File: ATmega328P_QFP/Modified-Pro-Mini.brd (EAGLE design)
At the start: 17.8 x 33 mm, 25 parts, among them Q1 8/16/20MHz, U1 ATMEGA328, U2 MIC5205

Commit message: updated silk
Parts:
- removed U$1: LOGO-SFESK, SparkFun:SFE-LOGO-FLAME
- removed U$11: LOGO-SFENEW, SparkFun:SFE-NEW-WEBLOGO
- removed U$3: OSHW-LOGOS, SparkFun:OSHW-LOGO-S
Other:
- board text removed: "Arduino Pro"
- board text removed: "Mini"
- board text removed: "www.arduino.cc"
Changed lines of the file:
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@@
 <grid distance="0.05" unitdist="inch" unit="inch" style="lines" multiple="1" display="yes" altdistance="0.005" altunitdist="inch" altunit="inch"/>
 <layers>
-<layer number="1" name="Top" color="4" fill="1" visible="yes" active="yes"/>
+<layer number="1" name="Top" color="4" fill="1" visible="no" active="yes"/>
 <layer number="2" name="Route2" color="1" fill="3" visible="no" active="no"/>
 <layer number="3" name="Route3" color="4" fill="3" visible="no" active="no"/>
@@
 <text x="1.27" y="30.734" size="0.8128" layer="21" ratio="15" rot="R90">BLK</text>
 <text x="17.272" y="30.734" size="0.8128" layer="21" ratio="15" rot="R90">GRN</text>
-<text x="6.5532" y="27.4574" size="0.8128" layer="21" ratio="15">Arduino Pro</text>
-<text x="8.636" y="28.575" size="0.8128" layer="21" ratio="15">Mini</text>
-<text x="4.191" y="6.858" size="1.778" layer="22" ratio="15" rot="MR90">www.arduino.cc</text>
 <text x="19.812" y="26.162" size="1.27" layer="27">Valid combinations:</text>
 <text x="19.812" y="23.622" size="1.27" layer="27">168V / 3.3V Reg / 8MHz</text>
@@
 <attribute name="VALUE" x="13.0556" y="0.9784" size="0.4064" layer="27" rot="R90"/>
 </element>
-<element name="U$11" library="SparkFun" package="SFE-NEW-WEBLOGO" value="LOGO-SFENEW" x="7.112" y="7.239" rot="MR90"/>
 <element name="U2" library="SparkFun" package="SOT23-5" value="MIC5205" x="8.89" y="24.1808" smashed="yes" rot="R90">
 <attribute name="NAME" x="6.731" y="23.2918" size="0.4064" layer="25" rot="R90"/>
@@
 <element name="JP6" library="SparkFun" package="1X12" value="" x="16.51" y="29.21" rot="MR270"/>
 <element name="JP7" library="SparkFun" package="1X12" value="" x="1.27" y="1.27" rot="MR90"/>
-<element name="U$1" library="SparkFun" package="SFE-LOGO-FLAME" value="LOGO-SFESK" x="4.064" y="6.985"/>
 <element name="JP2" library="SparkFun" package="1X02" value="" x="13.589" y="17.907" rot="MR90"/>
 <element name="U1" library="SparkFun" package="TQFP32-08" value="ATMEGA328" x="8.89" y="13.97" smashed="yes" rot="R315">
@@
 </element>
 <element name="JP1" library="SparkFun" package="1X06" value="FTDI Basic" x="15.24" y="31.75" rot="MR0"/>
-<element name="U$3" library="SparkFun" package="OSHW-LOGO-S" value="OSHW-LOGOS" x="12.5984" y="26.3906" rot="MR90"/>
 <element name="R1" library="SparkFun" package="0603-RES" value="" x="12.9794" y="23.1648" rot="MR90"/>
 <element name="R3" library="SparkFun" package="0603-RES" value="" x="14.2494" y="23.1648" rot="MR90"/>

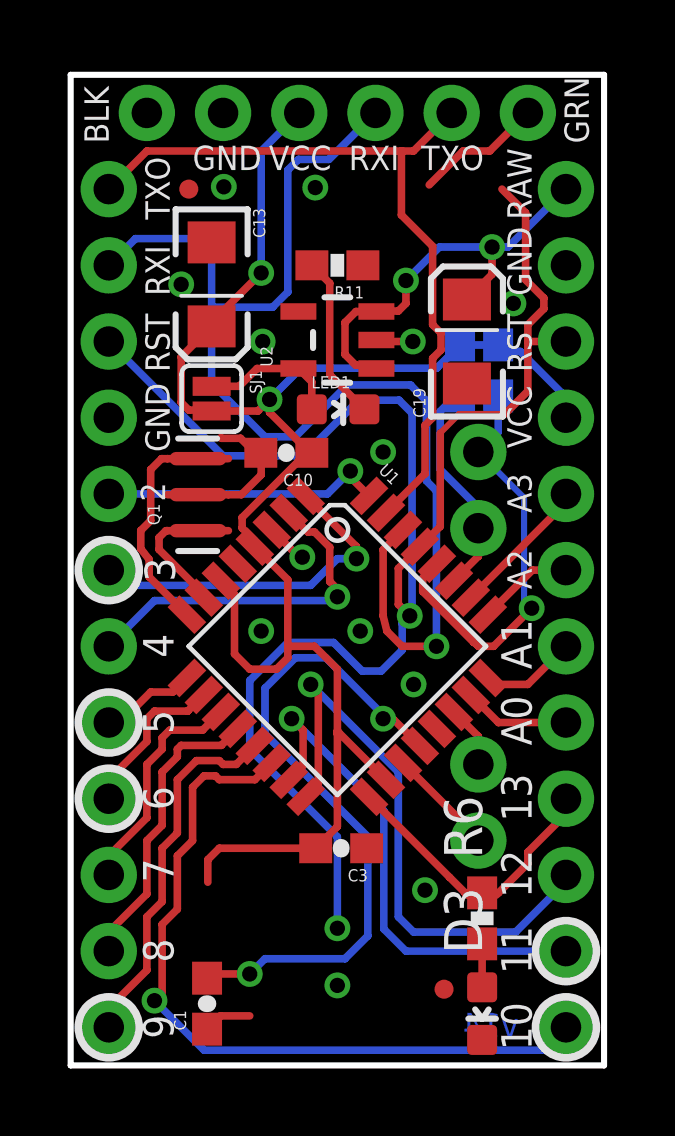
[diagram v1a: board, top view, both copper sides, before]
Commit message: removed power regulator
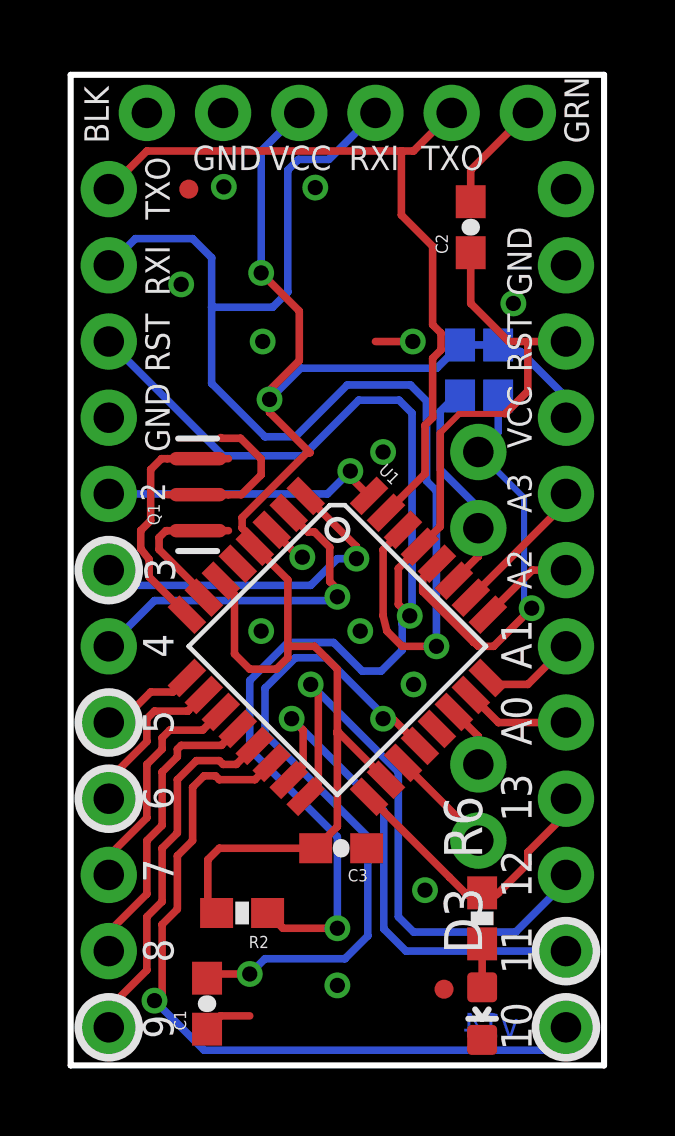
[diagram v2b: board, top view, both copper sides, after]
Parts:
- removed C10: 0.1uF, SparkFun:0603-CAP
- removed C13, C19: 10uF, SparkFun:EIA3216
- removed LED1: Red, Testing:0603-LED-ALT1
- removed R11: 10K, SparkFun:0603-RES
- removed SJ1: (no value), SparkFun-Passives:SJ_2S
- removed U2: MIC5205, SparkFun:SOT23-5
- added C2: 0.1uF, SparkFun:0603-CAP
- added R2: 10K, SparkFun:0603-RES
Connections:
- removed net N$3: LED1.A, SJ1.1, U2.5
- removed net N$4: LED1.C, R11.2
- removed net RAW: C19.A, JP6.1, U2.1, U2.3
- net DTR: now also C2.2
- net GND: no longer C10.2, C13.C, C19.C, R11.1, U2.2
- net RESET: now also C2.1, R2.1
- net VCC: now also R2.2; no longer C10.1, C13.A, SJ1.2
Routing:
- net RAW: track 14.1 -> 0.00 mm, vias 2 -> 0
- net N$4: track 5.53 -> 0.00 mm
- net N$3: track 4.68 -> 0.00 mm
- net VCC: track 57.4 -> 55.0 mm
- net RESET: track 55.6 -> 56.3 mm
- net DTR: track 4.28 -> 3.75 mm
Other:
- board text removed: "RAW"

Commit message: rerouted wires left by removed compoents
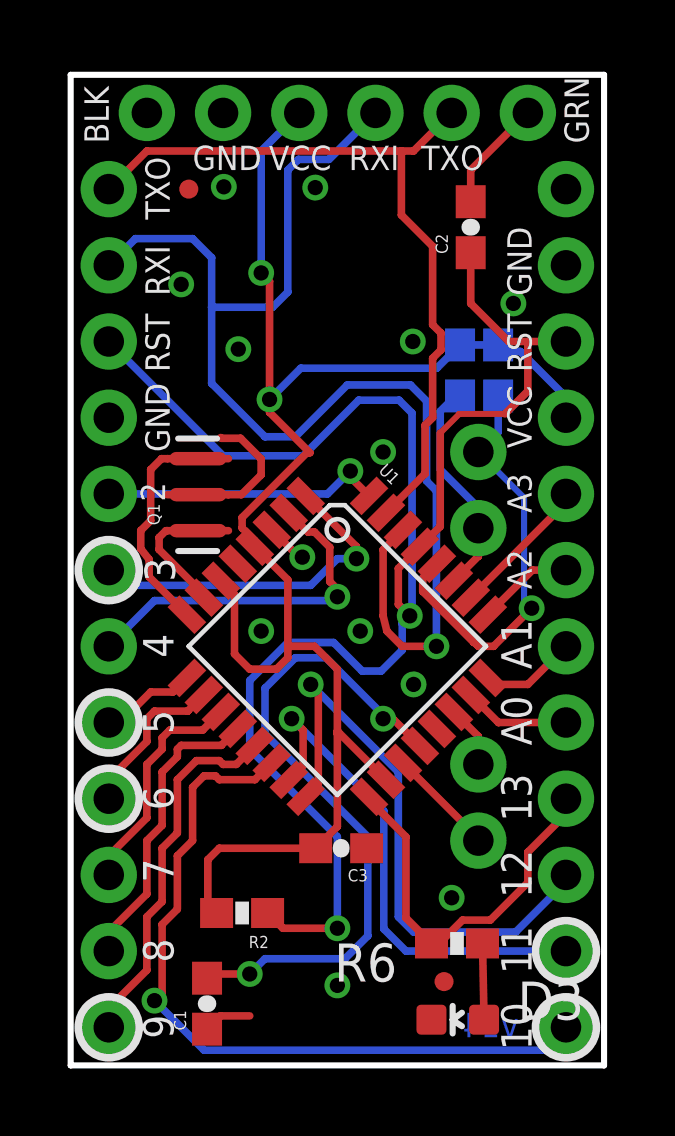
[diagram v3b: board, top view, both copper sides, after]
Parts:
- moved R6 1.19 mm to (12.9, 4.06), turned to 0 degrees
- moved D3 0.84 mm to (12.9, 1.52), turned to 90 degrees
- moved JP8 0.25 mm to (12.4, 2.79)
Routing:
- net SCK: track 9.93 -> 13.5 mm
- net GND: track 7.83 -> 6.59 mm
- net N$7: track 1.45 -> 2.54 mm
- net VCC: track 55.0 -> 54.4 mm
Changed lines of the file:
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@@
 <setting verticaltext="up"/>
 </settings>
-<grid distance="0.02" unitdist="inch" unit="inch" style="lines" multiple="1" display="yes" altdistance="0.005" altunitdist="inch" altunit="inch"/>
+<grid distance="0.01" unitdist="inch" unit="inch" style="lines" multiple="1" display="yes" altdistance="0.005" altunitdist="inch" altunit="inch"/>
 <layers>
 <layer number="1" name="Top" color="4" fill="1" visible="yes" active="yes"/>
@@
 <layer number="19" name="Unrouted" color="6" fill="1" visible="yes" active="yes"/>
 <layer number="20" name="Dimension" color="6" fill="1" visible="yes" active="yes"/>
-<layer number="21" name="tPlace" color="16" fill="1" visible="no" active="yes"/>
-<layer number="22" name="bPlace" color="14" fill="1" visible="no" active="yes"/>
+<layer number="21" name="tPlace" color="16" fill="1" visible="yes" active="yes"/>
+<layer number="22" name="bPlace" color="14" fill="1" visible="yes" active="yes"/>
 <layer number="23" name="tOrigins" color="15" fill="1" visible="yes" active="yes"/>
 <layer number="24" name="bOrigins" color="15" fill="1" visible="yes" active="yes"/>
@@
 <attribute name="VALUE" x="5.5372" y="1.2827" size="0.4064" layer="27" rot="R90"/>
 </element>
-<element name="R6" library="SparkFun" package="0603-RES" value="330" x="13.716" y="4.9022" smashed="yes" rot="R270">
-<attribute name="NAME" x="13.716" y="6.9022" size="1.27" layer="25" rot="R90"/>
-<attribute name="VALUE" x="13.081" y="4.5598" size="0.4064" layer="27" rot="R90"/>
+<element name="R6" library="SparkFun" package="0603-RES" value="330" x="12.8778" y="4.064" smashed="yes">
+<attribute name="NAME" x="10.8778" y="4.064" size="1.27" layer="25" rot="R180"/>
+<attribute name="VALUE" x="13.2202" y="3.429" size="0.4064" layer="27" rot="R180"/>
 </element>
-<element name="D3" library="Testing" package="0603-LED-ALT1" value="Green" x="13.716" y="1.7272" smashed="yes" rot="R180">
-<attribute name="NAME" x="13.716" y="3.7272" size="1.27" layer="25" rot="R90"/>
-<attribute name="VALUE" x="13.0556" y="0.9784" size="0.4064" layer="27" rot="R90"/>
+<element name="D3" library="Testing" package="0603-LED-ALT1" value="Green" x="12.9032" y="1.524" smashed="yes" rot="R90">
+<attribute name="NAME" x="14.9032" y="1.524" size="1.27" layer="25"/>
+<attribute name="VALUE" x="12.1544" y="2.1844" size="0.4064" layer="27"/>
 </element>
 <element name="JP6" library="SparkFun" package="1X12" value="" x="16.51" y="29.21" rot="MR270"/>
@@
 <element name="R3" library="SparkFun" package="0603-RES" value="" x="14.2494" y="23.1648" rot="MR90"/>
 <element name="JP5" library="SparkFun" package="MICRO-FIDUCIAL" value="FIDUCIALUFIDUCIAL" x="3.937" y="29.21"/>
-<element name="JP8" library="SparkFun" package="MICRO-FIDUCIAL" value="FIDUCIALUFIDUCIAL" x="12.446" y="2.54"/>
+<element name="JP8" library="SparkFun" package="MICRO-FIDUCIAL" value="FIDUCIALUFIDUCIAL" x="12.446" y="2.794"/>
 <element name="JP3" library="SparkFun" package="1X02" value="" x="13.589" y="7.493" rot="MR90"/>
 <element name="Q1" library="Testing" package="RESONATOR-SMD-1:1" value="8/16/20MHz" x="4.2418" y="19.0246" rot="R90"/>
@@
 <contactref element="JP1" pad="5"/>
 <contactref element="JP1" pad="6"/>
-<wire x1="11.4046" y1="24.13" x2="10.16" y2="24.13" width="0.254" layer="1"/>
 <via x="11.43" y="12.7" extent="1-16" drill="0.508"/>
 <via x="9.652" y="14.478" extent="1-16" drill="0.508"/>
@@
 <via x="3.683" y="26.035" extent="1-16" drill="0.508"/>
 <via x="11.4046" y="24.13" extent="1-16" drill="0.508"/>
-<via x="6.4008" y="24.13" extent="1-16" drill="0.508"/>
 <polygon width="0.254" layer="1" isolate="0.3048">
 <vertex x="0" y="33.02"/>
@@
 <wire x1="7.666053125" y1="16.891" x2="7.747" y2="16.891" width="0.254" layer="1"/>
 <via x="8.1534" y="29.2608" extent="1-16" drill="0.508"/>
-<via x="11.811" y="5.842" extent="1-16" drill="0.508"/>
 <contactref element="Q1" pad="2"/>
 <wire x1="5.2578" y1="19.0246" x2="5.6896" y2="19.0246" width="0.254" layer="1"/>
@@
 <wire x1="5.6642" y1="20.9042" x2="5.0292" y2="20.9042" width="0.254" layer="1"/>
 <wire x1="5.0292" y1="20.9042" x2="5.0038" y2="20.9296" width="0.254" layer="1"/>
+<via x="5.588" y="23.876" extent="1-16" drill="0.508"/>
+<via x="12.7" y="5.588" extent="1-16" drill="0.508"/>
 </signal>
 <signal name="AREF">
@@
 <wire x1="16.51" y1="8.382" x2="16.51" y2="8.89" width="0.254" layer="1"/>
 <wire x1="15.24" y1="7.112" x2="16.51" y2="8.382" width="0.254" layer="1"/>
-<wire x1="15.24" y1="6.731" x2="15.24" y2="7.112" width="0.254" layer="1"/>
-<wire x1="14.185" y1="5.676" x2="14.2612" y2="5.7522" width="0.254" layer="1"/>
-<wire x1="9.945425" y1="8.954771875" x2="12.6251" y2="6.275096875" width="0.254" layer="1"/>
-<wire x1="13.147996875" y1="5.7522" x2="13.224196875" y2="5.676" width="0.254" layer="1"/>
-<wire x1="13.716" y1="5.7522" x2="14.2612" y2="5.7522" width="0.254" layer="1"/>
-<wire x1="14.2612" y1="5.7522" x2="15.24" y2="6.731" width="0.254" layer="1"/>
-<wire x1="13.716" y1="5.7522" x2="13.147996875" y2="5.7522" width="0.254" layer="1"/>
-<wire x1="13.147996875" y1="5.7522" x2="12.6251" y2="6.275096875" width="0.254" layer="1"/>
+<wire x1="11.938" y1="4.1538" x2="12.0278" y2="4.064" width="0.254" layer="1"/>
+<wire x1="12.0278" y1="4.064" x2="12.28266875" y2="4.064" width="0.254" layer="1"/>
+<wire x1="9.945425" y1="8.954771875" x2="9.945425" y2="8.850575" width="0.254" layer="1"/>
+<wire x1="9.945425" y1="8.850575" x2="11.176" y2="7.62" width="0.254" layer="1"/>
+<wire x1="11.176" y1="7.62" x2="11.176" y2="4.9158" width="0.254" layer="1"/>
+<wire x1="11.176" y1="4.9158" x2="12.0278" y2="4.064" width="0.254" layer="1"/>
+<wire x1="13.06206875" y1="4.8434" x2="13.9874" y2="4.8434" width="0.254" layer="1"/>
+<wire x1="13.9874" y1="4.8434" x2="15.24" y2="6.096" width="0.254" layer="1"/>
+<wire x1="12.0278" y1="4.064" x2="12.28266875" y2="4.064" width="0.254" layer="1"/>
+<wire x1="12.28266875" y1="4.064" x2="13.06206875" y2="4.8434" width="0.254" layer="1"/>
+<wire x1="15.24" y1="6.096" x2="15.24" y2="7.112" width="0.254" layer="1"/>
 </signal>
 <signal name="MISO">
@@
 <contactref element="R6" pad="2"/>
 <contactref element="D3" pad="A"/>
-<wire x1="13.716" y1="2.6042" x2="13.716" y2="4.0522" width="0.254" layer="1"/>
+<wire x1="13.7802" y1="1.524" x2="13.7278" y2="4.064" width="0.254" layer="1"/>
 </signal>
 <signal name="TXO">
@@
 <wire x1="6.6294" y1="21.7678" x2="6.6294" y2="22.1996" width="0.254" layer="1"/>
 <wire x1="6.6294" y1="22.1996" x2="6.6294" y2="22.5044" width="0.254" layer="1"/>
-<wire x1="6.6294" y1="22.5044" x2="7.62" y2="23.495" width="0.254" layer="1"/>
-<wire x1="7.62" y1="23.495" x2="7.62" y2="25.146" width="0.254" layer="1"/>
-<wire x1="7.62" y1="25.146" x2="6.35" y2="26.416" width="0.254" layer="1"/>
 <contactref element="R2" pad="2"/>
 <wire x1="4.572" y1="6.858" x2="4.572" y2="5.373" width="0.254" layer="1"/>
 <wire x1="4.572" y1="5.373" x2="4.865" y2="5.08" width="0.254" layer="1"/>
 <wire x1="7.874" y1="20.4216" x2="7.9756" y2="20.4216" width="0.254" layer="1"/>
+<wire x1="6.6294" y1="22.1996" x2="6.6294" y2="26.1366" width="0.254" layer="1"/>
+<wire x1="6.6294" y1="26.1366" x2="6.35" y2="26.416" width="0.254" layer="1"/>
 </signal>
 <signal name="D9">

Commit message: changed raw pin to gnd
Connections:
- net GND: now also JP6.1
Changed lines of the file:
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@@
 <via x="5.588" y="23.876" extent="1-16" drill="0.508"/>
 <via x="12.7" y="5.588" extent="1-16" drill="0.508"/>
+<contactref element="JP6" pad="1"/>
 </signal>
 <signal name="AREF">

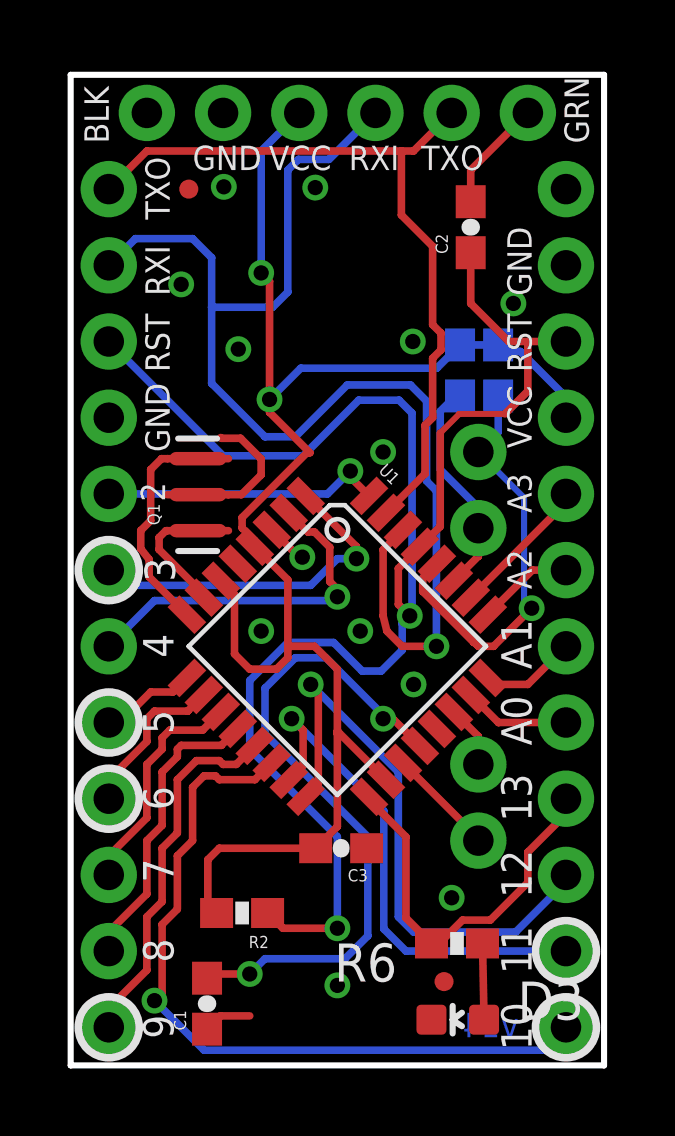
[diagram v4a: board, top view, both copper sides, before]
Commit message: bumbed out all sides by 0.01in
got board to pass OSH park DRC
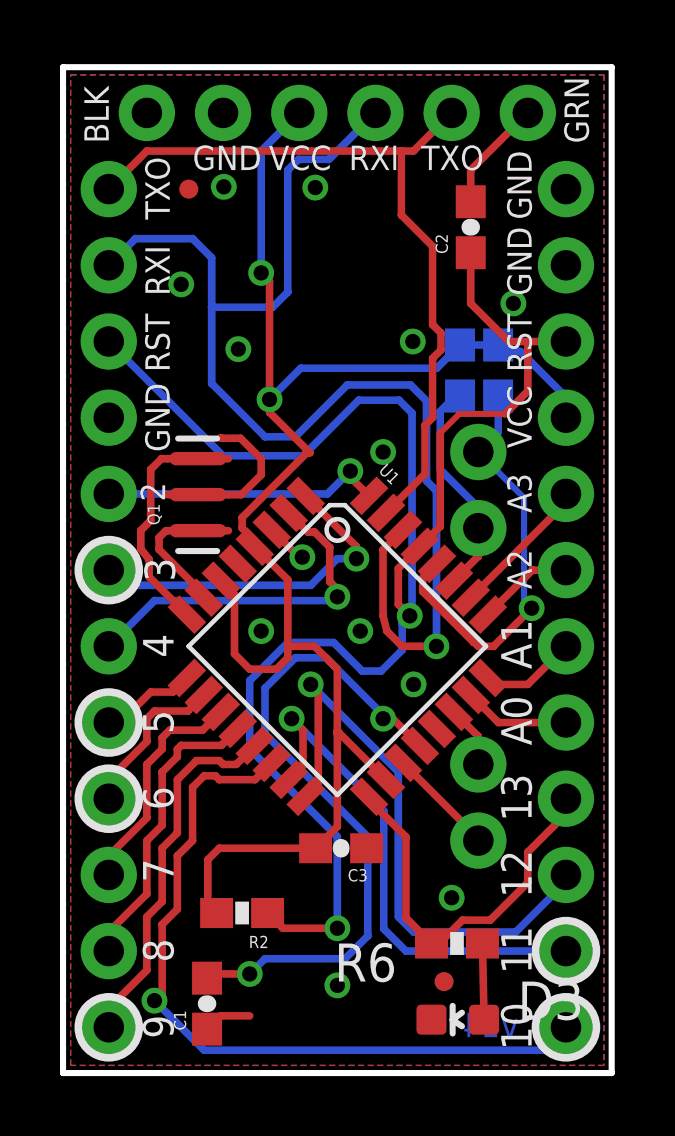
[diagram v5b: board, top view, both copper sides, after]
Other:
- board size 17.8 x 33 mm -> 18.3 x 33.5 mm
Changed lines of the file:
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@@
 <board>
 <plain>
-<wire x1="0" y1="33.02" x2="0" y2="0" width="0.2032" layer="20"/>
-<wire x1="0" y1="0" x2="17.78" y2="0" width="0.2032" layer="20"/>
-<wire x1="17.78" y1="0" x2="17.78" y2="33.02" width="0.2032" layer="20"/>
-<wire x1="17.78" y1="33.02" x2="0" y2="33.02" width="0.2032" layer="20"/>
+<wire x1="-0.254" y1="33.274" x2="-0.254" y2="-0.254" width="0.2032" layer="20"/>
+<wire x1="-0.254" y1="-0.254" x2="18.034" y2="-0.254" width="0.2032" layer="20"/>
+<wire x1="18.034" y1="-0.254" x2="18.034" y2="33.274" width="0.2032" layer="20"/>
+<wire x1="18.034" y1="33.274" x2="-0.254" y2="33.274" width="0.2032" layer="20"/>
 <wire x1="15.494" y1="0.508" x2="15.494" y2="29.21" width="0.0762" layer="51"/>
 <wire x1="3.429" y1="0.508" x2="3.429" y2="29.21" width="0.0762" layer="51"/>
@@
 <rectangle x1="6.604" y1="0.635" x2="7.239" y2="1.27" layer="22"/>
 <rectangle x1="5.334" y1="0.635" x2="5.969" y2="1.27" layer="22"/>
+<text x="15.367" y="28.194" size="0.8128" layer="21" ratio="15" rot="R90">GND</text>
 </plain>
 <attributes>
